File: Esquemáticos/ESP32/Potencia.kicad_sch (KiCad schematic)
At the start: 11 parts

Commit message: Cajas Potencia
lolololol
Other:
- note added: "Entrada de alimentación de 12V mediante un Jack"
- note added: "Etapa de regulación - Caídas de 12V a 5V y de 12V a 3.3V"
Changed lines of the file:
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@@
+    (stroke (width 0) (type default) (color 0 0 0 0))
+  )
+  (polyline (pts (xy 148.59 69.85) (xy 219.71 69.85))
     (stroke (width 0) (type default) (color 0 0 0 0))
   )
   (wire (pts (xy 190.5 88.9) (xy 207.01 88.9))
+    (stroke (width 0) (type default) (color 0 0 0 0))
+  )
+  (polyline (pts (xy 143.51 118.11) (xy 50.8 118.11))
     (stroke (width 0) (type default) (color 0 0 0 0))
   )
@@
   )
   (wire (pts (xy 163.83 138.43) (xy 163.83 143.51))
+    (stroke (width 0) (type default) (color 0 0 0 0))
+  )
+  (polyline (pts (xy 50.8 69.85) (xy 52.07 69.85))
+    (stroke (width 0) (type default) (color 0 0 0 0))
+  )
+  (polyline (pts (xy 219.71 153.67) (xy 219.71 69.85))
+    (stroke (width 0) (type default) (color 0 0 0 0))
+  )
+  (polyline (pts (xy 50.8 69.85) (xy 143.51 69.85))
     (stroke (width 0) (type default) (color 0 0 0 0))
   )
@@
     (stroke (width 0) (type default) (color 0 0 0 0))
   )
+  (polyline (pts (xy 148.59 153.67) (xy 219.71 153.67))
+    (stroke (width 0) (type default) (color 0 0 0 0))
+  )
+  (polyline (pts (xy 143.51 69.85) (xy 143.51 118.11))
+    (stroke (width 0) (type default) (color 0 0 0 0))
+  )
   (wire (pts (xy 182.88 143.51) (xy 182.88 144.78))
     (stroke (width 0) (type default) (color 0 0 0 0))
@@
   )
   (wire (pts (xy 207.01 83.82) (xy 207.01 88.9))
+    (stroke (width 0) (type default) (color 0 0 0 0))
+  )
+  (polyline (pts (xy 148.59 69.85) (xy 148.59 153.67))
     (stroke (width 0) (type default) (color 0 0 0 0))
   )
@@
     (stroke (width 0) (type default) (color 0 0 0 0))
   )
+  (polyline (pts (xy 50.8 118.11) (xy 50.8 69.85))
+    (stroke (width 0) (type default) (color 0 0 0 0))
+  )
   (wire (pts (xy 182.88 143.51) (xy 207.01 143.51))
     (stroke (width 0) (type default) (color 0 0 0 0))
   )
+  (text "Entrada de alimentación de 12V mediante un Jack " (at 76.2 123.19 0)
+    (effects (font (size 1.27 1.27)) (justify left bottom))
+  )
+  (text "Etapa de regulación - Caídas de 12V a 5V y de 12V a 3.3V"
+    (at 156.21 157.48 0)
+    (effects (font (size 1.27 1.27)) (justify left bottom))
+  )
   (text "Etapa de potencia" (at 186.69 190.5 0)

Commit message: Mas commits :sunglasses:
Agragados números de los componentes
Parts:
- gave numbers to parts that had none: 5
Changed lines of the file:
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@@
   (symbol (lib_id "Regulator_Linear:AMS1117-5.0") (at 182.88 88.9 0) (unit 1)
     (in_bom yes) (on_board yes) (fields_autoplaced)
-    (property "Reference" "U?" (id 0) (at 182.88 81.28 0))
+    (property "Reference" "U5" (id 0) (at 182.88 81.28 0))
     (property "Value" "AMS1117-5.0" (id 1) (at 182.88 83.82 0))
     (property "Footprint" "Package_TO_SOT_SMD:SOT-223-3_TabPin2" (id 2) (at 182.88 83.82 0)
@@
   (symbol (lib_id "Connector:Barrel_Jack") (at 64.77 91.44 0) (unit 1)
     (in_bom yes) (on_board yes) (fields_autoplaced)
-    (property "Reference" "J?" (id 0) (at 64.77 82.55 0))
+    (property "Reference" "J3" (id 0) (at 64.77 82.55 0))
     (property "Value" "Barrel_Jack" (id 1) (at 64.77 85.09 0))
     (property "Footprint" "" (id 2) (at 66.04 92.456 0)
@@
   (symbol (lib_id "Diode:1N4007") (at 109.22 88.9 180) (unit 1)
     (in_bom yes) (on_board yes) (fields_autoplaced)
-    (property "Reference" "D?" (id 0) (at 109.22 82.55 0))
+    (property "Reference" "D3" (id 0) (at 109.22 82.55 0))
     (property "Value" "1N4007" (id 1) (at 109.22 85.09 0))
     (property "Footprint" "Diode_THT:D_DO-41_SOD81_P10.16mm_Horizontal" (id 2) (at 109.22 84.455 0)
@@
   (symbol (lib_id "power:GND") (at 128.27 107.95 0) (unit 1)
     (in_bom yes) (on_board yes) (fields_autoplaced)
-    (property "Reference" "#PWR?" (id 0) (at 128.27 114.3 0)
+    (property "Reference" "#PWR03" (id 0) (at 128.27 114.3 0)
       (effects (font (size 1.27 1.27)) hide)
     )
@@
   (symbol (lib_id "power:GND") (at 182.88 105.41 0) (unit 1)
     (in_bom yes) (on_board yes) (fields_autoplaced)
-    (property "Reference" "#PWR?" (id 0) (at 182.88 111.76 0)
+    (property "Reference" "#PWR04" (id 0) (at 182.88 111.76 0)
       (effects (font (size 1.27 1.27)) hide)
     )
@@
   (symbol (lib_id "Regulator_Linear:AMS1117-3.3") (at 182.88 128.27 0) (unit 1)
     (in_bom yes) (on_board yes) (fields_autoplaced)
-    (property "Reference" "U?" (id 0) (at 182.88 120.65 0))
+    (property "Reference" "U6" (id 0) (at 182.88 120.65 0))
     (property "Value" "AMS1117-3.3" (id 1) (at 182.88 123.19 0))
     (property "Footprint" "Package_TO_SOT_SMD:SOT-223-3_TabPin2" (id 2) (at 182.88 123.19 0)
@@
   (symbol (lib_id "power:Earth") (at 78.74 107.95 0) (unit 1)
     (in_bom yes) (on_board yes) (fields_autoplaced)
-    (property "Reference" "#PWR?" (id 0) (at 78.74 114.3 0)
+    (property "Reference" "#PWR01" (id 0) (at 78.74 114.3 0)
       (effects (font (size 1.27 1.27)) hide)
     )
@@
   (symbol (lib_id "power:GND") (at 182.88 144.78 0) (unit 1)
     (in_bom yes) (on_board yes) (fields_autoplaced)
-    (property "Reference" "#PWR?" (id 0) (at 182.88 151.13 0)
+    (property "Reference" "#PWR05" (id 0) (at 182.88 151.13 0)
       (effects (font (size 1.27 1.27)) hide)
     )
@@
   (symbol (lib_id "power:GND") (at 113.03 107.95 0) (unit 1)
     (in_bom yes) (on_board yes) (fields_autoplaced)
-    (property "Reference" "#PWR?" (id 0) (at 113.03 114.3 0)
+    (property "Reference" "#PWR02" (id 0) (at 113.03 114.3 0)
       (effects (font (size 1.27 1.27)) hide)
     )
@@
   (symbol (lib_id "Switch:SW_DIP_x01") (at 88.9 88.9 0) (unit 1)
     (in_bom yes) (on_board yes) (fields_autoplaced)
-    (property "Reference" "SW?" (id 0) (at 88.9 81.28 0))
+    (property "Reference" "SW1" (id 0) (at 88.9 81.28 0))
     (property "Value" "SW_DIP_x01" (id 1) (at 88.9 83.82 0))
     (property "Footprint" "" (id 2) (at 88.9 88.9 0)

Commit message: auxilio
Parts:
- J1: renamed from J3; footprint (none) -> Connector_BarrelJack:BarrelJack_CLIFF_FC681465S_SMT_Horizontal
- renumbered D3 to D?, U5 to U?, U6 to U?
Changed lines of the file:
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@@
   (symbol (lib_id "Regulator_Linear:AMS1117-5.0") (at 182.88 88.9 0) (unit 1)
     (in_bom yes) (on_board yes) (fields_autoplaced)
-    (property "Reference" "U5" (id 0) (at 182.88 81.28 0))
+    (property "Reference" "U?" (id 0) (at 182.88 81.28 0))
     (property "Value" "AMS1117-5.0" (id 1) (at 182.88 83.82 0))
     (property "Footprint" "Package_TO_SOT_SMD:SOT-223-3_TabPin2" (id 2) (at 182.88 83.82 0)
@@
   (symbol (lib_id "Connector:Barrel_Jack") (at 64.77 91.44 0) (unit 1)
     (in_bom yes) (on_board yes) (fields_autoplaced)
-    (property "Reference" "J3" (id 0) (at 64.77 82.55 0))
+    (property "Reference" "J1" (id 0) (at 64.77 82.55 0))
     (property "Value" "Barrel_Jack" (id 1) (at 64.77 85.09 0))
-    (property "Footprint" "" (id 2) (at 66.04 92.456 0)
+    (property "Footprint" "Connector_BarrelJack:BarrelJack_CLIFF_FC681465S_SMT_Horizontal" (id 2) (at 66.04 92.456 0)
       (effects (font (size 1.27 1.27)) hide)
     )
@@
   (symbol (lib_id "Diode:1N4007") (at 109.22 88.9 180) (unit 1)
     (in_bom yes) (on_board yes) (fields_autoplaced)
-    (property "Reference" "D3" (id 0) (at 109.22 82.55 0))
+    (property "Reference" "D?" (id 0) (at 109.22 82.55 0))
     (property "Value" "1N4007" (id 1) (at 109.22 85.09 0))
     (property "Footprint" "Diode_THT:D_DO-41_SOD81_P10.16mm_Horizontal" (id 2) (at 109.22 84.455 0)
@@
   (symbol (lib_id "power:GND") (at 128.27 107.95 0) (unit 1)
     (in_bom yes) (on_board yes) (fields_autoplaced)
-    (property "Reference" "#PWR03" (id 0) (at 128.27 114.3 0)
+    (property "Reference" "#PWR?" (id 0) (at 128.27 114.3 0)
       (effects (font (size 1.27 1.27)) hide)
     )
@@
   (symbol (lib_id "power:GND") (at 182.88 105.41 0) (unit 1)
     (in_bom yes) (on_board yes) (fields_autoplaced)
-    (property "Reference" "#PWR04" (id 0) (at 182.88 111.76 0)
+    (property "Reference" "#PWR?" (id 0) (at 182.88 111.76 0)
       (effects (font (size 1.27 1.27)) hide)
     )
@@
   (symbol (lib_id "Regulator_Linear:AMS1117-3.3") (at 182.88 128.27 0) (unit 1)
     (in_bom yes) (on_board yes) (fields_autoplaced)
-    (property "Reference" "U6" (id 0) (at 182.88 120.65 0))
+    (property "Reference" "U?" (id 0) (at 182.88 120.65 0))
     (property "Value" "AMS1117-3.3" (id 1) (at 182.88 123.19 0))
     (property "Footprint" "Package_TO_SOT_SMD:SOT-223-3_TabPin2" (id 2) (at 182.88 123.19 0)
@@
   (symbol (lib_id "power:Earth") (at 78.74 107.95 0) (unit 1)
     (in_bom yes) (on_board yes) (fields_autoplaced)
-    (property "Reference" "#PWR01" (id 0) (at 78.74 114.3 0)
+    (property "Reference" "#PWR?" (id 0) (at 78.74 114.3 0)
       (effects (font (size 1.27 1.27)) hide)
     )
@@
   (symbol (lib_id "power:GND") (at 182.88 144.78 0) (unit 1)
     (in_bom yes) (on_board yes) (fields_autoplaced)
-    (property "Reference" "#PWR05" (id 0) (at 182.88 151.13 0)
+    (property "Reference" "#PWR?" (id 0) (at 182.88 151.13 0)
       (effects (font (size 1.27 1.27)) hide)
     )
@@
   (symbol (lib_id "power:GND") (at 113.03 107.95 0) (unit 1)
     (in_bom yes) (on_board yes) (fields_autoplaced)
-    (property "Reference" "#PWR02" (id 0) (at 113.03 114.3 0)
-      (effects (font (size 1.27 1.27)) hide)
-    )
+    (property "Reference" "#PWR?" (id 0) (at 113.03 114.3 0)
+      (effects (font (size 1.27 1.27)) hide)
+    )

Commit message: Support
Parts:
- gave numbers to parts that had none: 3
- renumbered J1 to J3
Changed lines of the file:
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@@
   (symbol (lib_id "Regulator_Linear:AMS1117-5.0") (at 182.88 88.9 0) (unit 1)
     (in_bom yes) (on_board yes) (fields_autoplaced)
-    (property "Reference" "U?" (id 0) (at 182.88 81.28 0))
+    (property "Reference" "U5" (id 0) (at 182.88 81.28 0))
     (property "Value" "AMS1117-5.0" (id 1) (at 182.88 83.82 0))
     (property "Footprint" "Package_TO_SOT_SMD:SOT-223-3_TabPin2" (id 2) (at 182.88 83.82 0)
@@
   (symbol (lib_id "Connector:Barrel_Jack") (at 64.77 91.44 0) (unit 1)
     (in_bom yes) (on_board yes) (fields_autoplaced)
-    (property "Reference" "J1" (id 0) (at 64.77 82.55 0))
+    (property "Reference" "J3" (id 0) (at 64.77 82.55 0))
     (property "Value" "Barrel_Jack" (id 1) (at 64.77 85.09 0))
     (property "Footprint" "Connector_BarrelJack:BarrelJack_CLIFF_FC681465S_SMT_Horizontal" (id 2) (at 66.04 92.456 0)
@@
   (symbol (lib_id "Diode:1N4007") (at 109.22 88.9 180) (unit 1)
     (in_bom yes) (on_board yes) (fields_autoplaced)
-    (property "Reference" "D?" (id 0) (at 109.22 82.55 0))
+    (property "Reference" "D3" (id 0) (at 109.22 82.55 0))
     (property "Value" "1N4007" (id 1) (at 109.22 85.09 0))
     (property "Footprint" "Diode_THT:D_DO-41_SOD81_P10.16mm_Horizontal" (id 2) (at 109.22 84.455 0)
@@
   (symbol (lib_id "power:GND") (at 128.27 107.95 0) (unit 1)
     (in_bom yes) (on_board yes) (fields_autoplaced)
-    (property "Reference" "#PWR?" (id 0) (at 128.27 114.3 0)
+    (property "Reference" "#PWR03" (id 0) (at 128.27 114.3 0)
       (effects (font (size 1.27 1.27)) hide)
     )
@@
   (symbol (lib_id "power:GND") (at 182.88 105.41 0) (unit 1)
     (in_bom yes) (on_board yes) (fields_autoplaced)
-    (property "Reference" "#PWR?" (id 0) (at 182.88 111.76 0)
+    (property "Reference" "#PWR04" (id 0) (at 182.88 111.76 0)
       (effects (font (size 1.27 1.27)) hide)
     )
@@
   (symbol (lib_id "Regulator_Linear:AMS1117-3.3") (at 182.88 128.27 0) (unit 1)
     (in_bom yes) (on_board yes) (fields_autoplaced)
-    (property "Reference" "U?" (id 0) (at 182.88 120.65 0))
+    (property "Reference" "U6" (id 0) (at 182.88 120.65 0))
     (property "Value" "AMS1117-3.3" (id 1) (at 182.88 123.19 0))
     (property "Footprint" "Package_TO_SOT_SMD:SOT-223-3_TabPin2" (id 2) (at 182.88 123.19 0)
@@
   (symbol (lib_id "power:Earth") (at 78.74 107.95 0) (unit 1)
     (in_bom yes) (on_board yes) (fields_autoplaced)
-    (property "Reference" "#PWR?" (id 0) (at 78.74 114.3 0)
+    (property "Reference" "#PWR01" (id 0) (at 78.74 114.3 0)
       (effects (font (size 1.27 1.27)) hide)
     )
@@
   (symbol (lib_id "power:GND") (at 182.88 144.78 0) (unit 1)
     (in_bom yes) (on_board yes) (fields_autoplaced)
-    (property "Reference" "#PWR?" (id 0) (at 182.88 151.13 0)
+    (property "Reference" "#PWR05" (id 0) (at 182.88 151.13 0)
       (effects (font (size 1.27 1.27)) hide)
     )
@@
   (symbol (lib_id "power:GND") (at 113.03 107.95 0) (unit 1)
     (in_bom yes) (on_board yes) (fields_autoplaced)
-    (property "Reference" "#PWR?" (id 0) (at 113.03 114.3 0)
-      (effects (font (size 1.27 1.27)) hide)
-    )
+    (property "Reference" "#PWR02" (id 0) (at 113.03 114.3 0)
+      (effects (font (size 1.27 1.27)) hide)
+    )

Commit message: Potencia Cap
xd?
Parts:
- C10, C13, C14, C15: footprint (none) -> Capacitor_SMD:C_0603_1608Metric_Pad1.08x0.95mm_HandSolder
- C12: footprint (none) -> Capacitor_SMD:C_1206_3216Metric_Pad1.33x1.80mm_HandSolder
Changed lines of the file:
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@@
       (effects (font (size 1.27 1.27)) (justify left))
     )
-    (property "Footprint" "" (id 2) (at 207.01 95.25 0)
+    (property "Footprint" "Capacitor_SMD:C_0603_1608Metric_Pad1.08x0.95mm_HandSolder" (id 2) (at 207.01 95.25 0)
       (effects (font (size 1.27 1.27)) hide)
     )
@@
       (effects (font (size 1.27 1.27)) (justify left))
     )
-    (property "Footprint" "" (id 2) (at 160.02 95.25 0)
+    (property "Footprint" "Capacitor_SMD:C_1206_3216Metric_Pad1.33x1.80mm_HandSolder" (id 2) (at 160.02 95.25 0)
       (effects (font (size 1.27 1.27)) hide)
     )
@@
       (effects (font (size 1.27 1.27)) (justify left))
     )
-    (property "Footprint" "" (id 2) (at 207.01 134.62 0)
+    (property "Footprint" "Capacitor_SMD:C_0603_1608Metric_Pad1.08x0.95mm_HandSolder" (id 2) (at 207.01 134.62 0)
       (effects (font (size 1.27 1.27)) hide)
     )
@@
       (effects (font (size 1.27 1.27)) (justify left))
     )
-    (property "Footprint" "" (id 2) (at 163.83 134.62 0)
+    (property "Footprint" "Capacitor_SMD:C_0603_1608Metric_Pad1.08x0.95mm_HandSolder" (id 2) (at 163.83 134.62 0)
       (effects (font (size 1.27 1.27)) hide)
     )
@@
       (effects (font (size 1.27 1.27)) (justify left))
     )
-    (property "Footprint" "" (id 2) (at 113.9952 101.6 0)
+    (property "Footprint" "Capacitor_SMD:C_0603_1608Metric_Pad1.08x0.95mm_HandSolder" (id 2) (at 113.9952 101.6 0)
       (effects (font (size 1.27 1.27)) hide)
     )

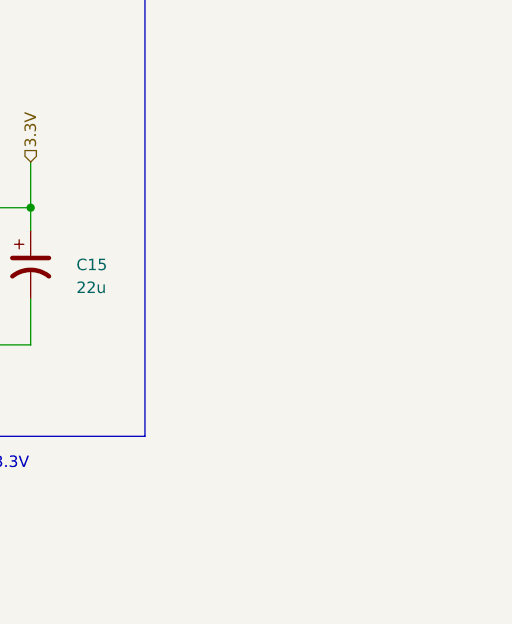
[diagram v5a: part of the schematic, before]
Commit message: me falta el led de programacion
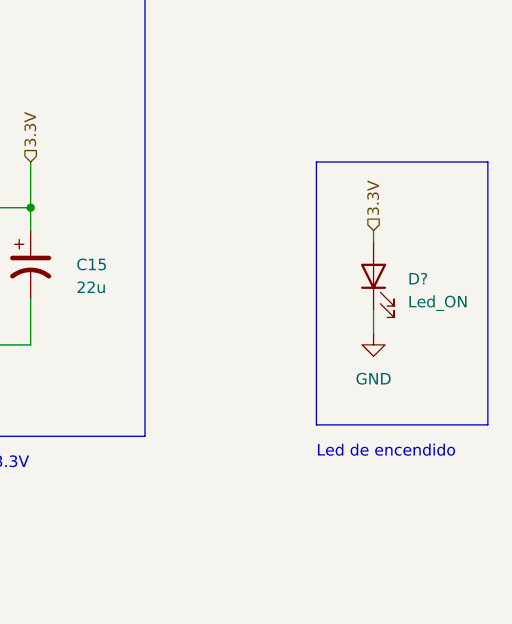
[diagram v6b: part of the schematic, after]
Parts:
- added D?: Led_ON, LED_SMD:LED_1206_3216Metric, symbol LED:IR26-21C_L110_TR8
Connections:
- net 3.3V: now also D?.2 (A)
- net GND: now also D?.1 (K)
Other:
- note added: "Led de encendido"
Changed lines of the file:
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@@
+    (stroke (width 0) (type default) (color 0 0 0 0))
+  )
+  (polyline (pts (xy 238.76 123.19) (xy 238.76 152.4))
     (stroke (width 0) (type default) (color 0 0 0 0))
   )
@@
     (stroke (width 0) (type default) (color 0 0 0 0))
   )
+  (polyline (pts (xy 257.81 152.4) (xy 257.81 123.19))
+    (stroke (width 0) (type default) (color 0 0 0 0))
+  )
   (wire (pts (xy 163.83 138.43) (xy 163.83 143.51))
     (stroke (width 0) (type default) (color 0 0 0 0))
@@
     (stroke (width 0) (type default) (color 0 0 0 0))
   )
+  (polyline (pts (xy 238.76 123.19) (xy 257.81 123.19))
+    (stroke (width 0) (type default) (color 0 0 0 0))
+  )
+  (wire (pts (xy 245.11 139.7) (xy 245.11 142.24))
+    (stroke (width 0) (type default) (color 0 0 0 0))
+  )
   (wire (pts (xy 207.01 91.44) (xy 207.01 88.9))
     (stroke (width 0) (type default) (color 0 0 0 0))
@@
     (stroke (width 0) (type default) (color 0 0 0 0))
   )
+  (wire (pts (xy 245.11 130.81) (xy 245.11 132.08))
+    (stroke (width 0) (type default) (color 0 0 0 0))
+  )
   (wire (pts (xy 163.83 120.65) (xy 163.83 128.27))
     (stroke (width 0) (type default) (color 0 0 0 0))
@@
     (stroke (width 0) (type default) (color 0 0 0 0))
   )
+  (polyline (pts (xy 238.76 152.4) (xy 257.81 152.4))
+    (stroke (width 0) (type default) (color 0 0 0 0))
+  )
   (wire (pts (xy 160.02 88.9) (xy 160.02 91.44))
     (stroke (width 0) (type default) (color 0 0 0 0))
@@
   )
   (text "Entrada de alimentación de 12V mediante un Jack " (at 76.2 123.19 0)
+    (effects (font (size 1.27 1.27)) (justify left bottom))
+  )
+  (text "Led de encendido\n" (at 238.76 156.21 0)
     (effects (font (size 1.27 1.27)) (justify left bottom))
   )
@@
   )
   (hierarchical_label "3.3V" (shape input) (at 207.01 123.19 90)
+    (effects (font (size 1.27 1.27)) (justify left))
+  )
+  (hierarchical_label "3.3V" (shape input) (at 245.11 130.81 90)
     (effects (font (size 1.27 1.27)) (justify left))
   )
@@
     (pin "1")
   )
+  (symbol (lib_id "LED:IR26-21C_L110_TR8") (at 245.11 135.89 90) (unit 1)
+    (in_bom yes) (on_board yes) (fields_autoplaced)
+    (property "Reference" "D?" (id 0) (at 248.92 136.2074 90)
+      (effects (font (size 1.27 1.27)) (justify right))
+    )
+    (property "Value" "Led_ON" (id 1) (at 248.92 138.7474 90)
+      (effects (font (size 1.27 1.27)) (justify right))
+    )
+    (property "Footprint" "LED_SMD:LED_1206_3216Metric" (id 2) (at 240.03 135.89 0)
+      (effects (font (size 1.27 1.27)) hide)
+    )
+    (property "Datasheet" "http://www.everlight.com/file/ProductFile/IR26-21C-L110-TR8.pdf" (id 3) (at 245.11 135.89 0)
+      (effects (font (size 1.27 1.27)) hide)
+    )
+    (pin "1")
+    (pin "2")
+  )
   (symbol (lib_id "Device:C_Polarized_US") (at 163.83 134.62 0) (unit 1)
     (in_bom yes) (on_board yes)
@@
       (effects (font (size 1.27 1.27)) hide)
     )
+    (pin "1")
+  )
+  (symbol (lib_id "power:GND") (at 245.11 142.24 0) (unit 1)
+    (in_bom yes) (on_board yes) (fields_autoplaced)
+    (property "Reference" "#PWR?" (id 0) (at 245.11 148.59 0)
+      (effects (font (size 1.27 1.27)) hide)
+    )
+    (property "Value" "GND" (id 1) (at 245.11 147.32 0))
+    (property "Footprint" "" (id 2) (at 245.11 142.24 0)
+      (effects (font (size 1.27 1.27)) hide)
+    )
+    (property "Datasheet" "" (id 3) (at 245.11 142.24 0)
+      (effects (font (size 1.27 1.27)) hide)
+    )

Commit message: Asignación Huellas de Resistencias
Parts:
- SW1: footprint (none) -> Button_Switch_SMD:SW_DIP_SPSTx01_Slide_6.7x4.1mm_W6.73mm_P2.54mm_LowProfile_JPin
- gave numbers to parts that had none: 1
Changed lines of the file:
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@@
   (symbol (lib_id "LED:IR26-21C_L110_TR8") (at 245.11 135.89 90) (unit 1)
     (in_bom yes) (on_board yes) (fields_autoplaced)
-    (property "Reference" "D?" (id 0) (at 248.92 136.2074 90)
+    (property "Reference" "D1" (id 0) (at 248.92 136.2074 90)
       (effects (font (size 1.27 1.27)) (justify right))
     )
@@
   (symbol (lib_id "power:GND") (at 245.11 142.24 0) (unit 1)
     (in_bom yes) (on_board yes) (fields_autoplaced)
-    (property "Reference" "#PWR?" (id 0) (at 245.11 148.59 0)
+    (property "Reference" "#PWR0101" (id 0) (at 245.11 148.59 0)
       (effects (font (size 1.27 1.27)) hide)
     )
@@
     (property "Reference" "SW1" (id 0) (at 88.9 81.28 0))
     (property "Value" "SW_DIP_x01" (id 1) (at 88.9 83.82 0))
-    (property "Footprint" "" (id 2) (at 88.9 88.9 0)
+    (property "Footprint" "Button_Switch_SMD:SW_DIP_SPSTx01_Slide_6.7x4.1mm_W6.73mm_P2.54mm_LowProfile_JPin" (id 2) (at 88.9 88.9 0)
       (effects (font (size 1.27 1.27)) hide)
     )
